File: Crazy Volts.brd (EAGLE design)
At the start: 100 x 80 mm, 3 parts, among them U1 ATMEGA328P-PU

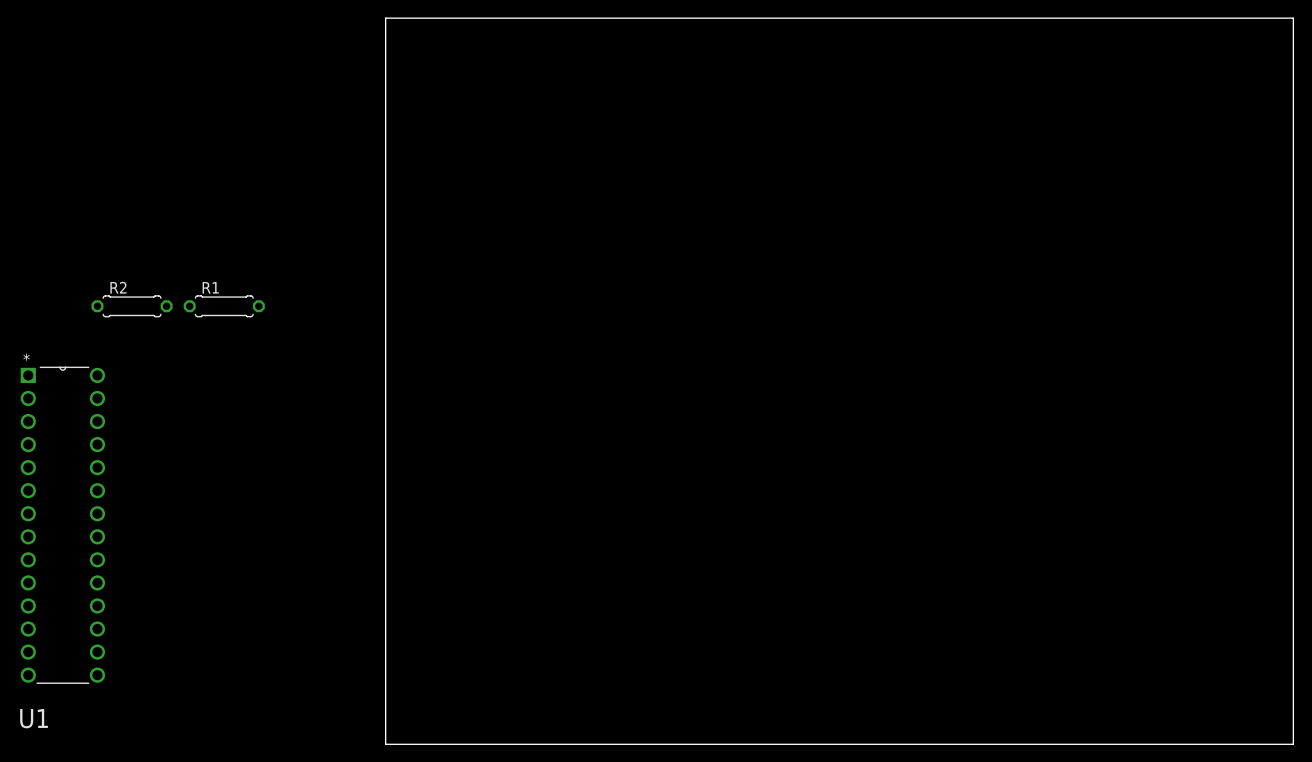
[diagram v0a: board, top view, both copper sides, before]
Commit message: final board; initial timekeeper
using a teensy + batt + xtal for timekeeping
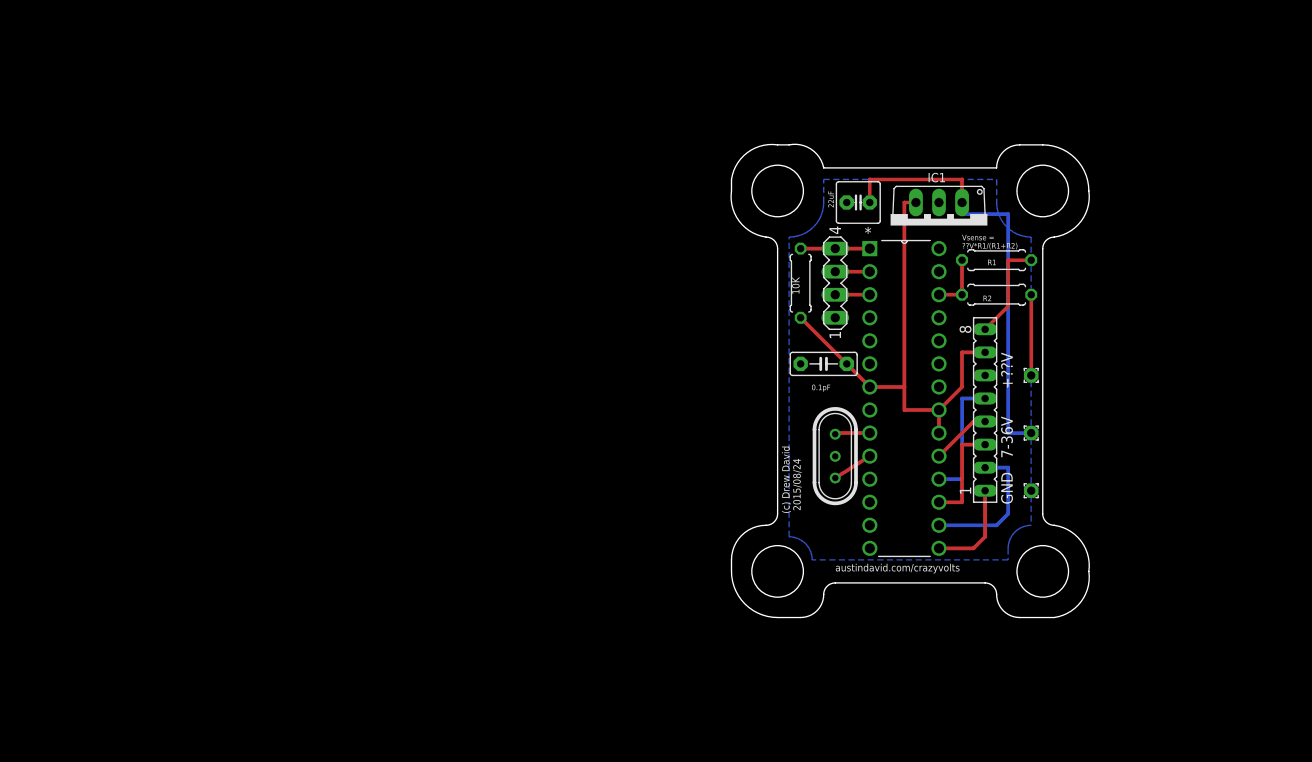
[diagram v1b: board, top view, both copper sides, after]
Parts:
- added +??V, 7-36V, GND: (no value), wirepad:1,6/0,9
- added 10K: 10k, rcl:0207/7
- added C1: 0.1pF, capacitor-wima:C5B2.5
- added C2: 22uF, capacitor-wima:C2.5-5
- added IC1: 7805TV, linear:TO220V
- added QF1: 8M10AHC49T, crystal:HC49U
- added SV1: (no value), con-lsta:FE08
- added SV2: (no value), con-lstb:MA04-1
- R1: value 50k -> R1
- R2: value 10k -> R2
- moved R2 95.3 mm to (67.3, 49.5), turned to 180 degrees
- moved U1 93.8 mm to (61.0, 21.6)
- moved R1 85.2 mm to (67.3, 53.3)
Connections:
- removed net AVCC: U1.20
- removed net N$1: U1.7
- removed net N$3: U1.21
- new net 3V3: SV1.6
- new net DISP_CLK: SV1.2, U1.16
- new net DISP_CS: SV1.5, U1.18
- new net DISP_DATA: SV1.1, U1.15
- new net DISP_DC: SV1.3, U1.17
- new net DISP_RST: SV1.4, U1.19
- new net IC10: QF1.1, U1.10
- new net IC9: QF1.3, U1.9
- new net RST: 10K.2, SV2.4, U1.1
- new net RX: SV2.3, U1.2
- new net TX: SV2.2, U1.3
- new net VCC: 10K.1, C1.1, IC1.3, SV1.7, U1.20, U1.21, U1.7
- new net VIN: 7-36V.1, C2.1, IC1.1
- net GND: now also C1.2, C2.2, GND.1, IC1.2, QF1.2, R1.2, SV1.8, SV2.1, U1.8; no longer R2.2
- net VBATT: now also +??V.1, R2.1; no longer R1.1
- net VSENSE: now also R1.1, R2.2, U1.26; no longer R1.2, R2.1
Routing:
- net VCC: track 0.00 -> 55.0 mm
- net VIN: track 0.00 -> 47.0 mm
- net DISP_CLK: track 0.00 -> 15.8 mm
- net DISP_CS: track 0.00 -> 14.0 mm
- net DISP_DC: track 0.00 -> 11.4 mm
- net GND: track 0.00 -> 11.2 mm
- net DISP_DATA: track 0.00 -> 10.7 mm
- net VBATT: track 0.00 -> 8.89 mm
- net RST: track 0.00 -> 7.62 mm
- net DISP_RST: track 0.00 -> 6.66 mm
- net VSENSE: track 0.00 -> 6.35 mm
- net IC10: track 0.00 -> 4.51 mm
- net IC9: track 0.00 -> 3.94 mm
- net RX: track 0.00 -> 3.81 mm
- net TX: track 0.00 -> 2.54 mm
- added copper zone on layer 16, net GND
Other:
- board size 100 x 80 mm -> 39.5 x 52.1 mm
- board text added: "(c) Drew David 2015/08/24"
- board text added: "CLK RST NC GND"
- board text added: "DATA DC CS VIN"
- board text added: "Vsense = ??V*R1/(R1+R2)"
- board text added: "austindavid.com/crazyvolts"
